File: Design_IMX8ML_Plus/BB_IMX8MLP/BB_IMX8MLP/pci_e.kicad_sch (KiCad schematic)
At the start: 0 parts

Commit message: Add SPB228 WIFI/BLE module
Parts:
- added J8: Bus_PCI_Express_Mini, Connector_PCBEdge:BUS_PCI_Express_Mini, symbol Connector:Bus_PCI_Express_Mini
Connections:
- new net: J8.15 (GND), J8.18 (GND), J8.21 (GND), J8.26 (GND), J8.27 (GND), J8.29 (GND), J8.34 (GND), J8.35 (GND), J8.37 (GND), J8.4 (GND), J8.40 (GND), J8.43 (GND), J8.50 (GND), J8.9 (GND)
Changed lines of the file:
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@@
-(kicad_sch (version 20230121) (generator eeschema)
-  (paper "A4")
+(kicad_sch
+	(version 20231120)
+	(generator "eeschema")
+	(generator_version "8.0")
+	(paper "A4")
+	(symbol
+		(lib_id "Connector:Bus_PCI_Express_Mini")
+		(at 167.64 107.95 0)
+		(unit 1)
+		(exclude_from_sim no)
+		(in_bom yes)
+		(on_board yes)
+		(dnp no)
+		(fields_autoplaced yes)
+		(property "Reference" "J8"
+			(at 172.3741 138.43 0)
+			(effects
+				(font
+					(size 1.27 1.27)
+				)
+				(justify left)
+			)
+		)
+		(property "Value" "Bus_PCI_Express_Mini"
+			(at 172.3741 140.97 0)
+			(effects
+				(font
+					(size 1.27 1.27)
+				)
+				(justify left)
+			)
+		)
+		(property "Footprint" "Connector_PCBEdge:BUS_PCI_Express_Mini"
+			(at 167.64 107.95 0)
+			(effects
+				(font
+					(size 1.27 1.27)
+				)
+				(hide yes)
+			)
+		)
+		(property "Datasheet" "0679105700"
+			(at 163.83 137.16 0)
+			(effects
+				(font
+					(size 1.27 1.27)
+				)
+				(hide yes)
+			)
+		)
+		(property "Description" "Mini-PCI Express bus connector"
+			(at 167.64 107.95 0)
+			(effects
+				(font
+					(size 1.27 1.27)
+				)
+				(hide yes)
+			)
+		)
+		(pin "23"
+		)
+		(pin "34"
+		)
+		(pin "30"
+		)
+		(pin "MP"
+		)
+		(pin "43"
+		)
+		(pin "20"
+		)
+		(pin "24"
+		)
+		(pin "9"
+		)
+		(pin "7"
+		)
+		(pin "45"
+		)
+		(pin "17"
+		)
+		(pin "44"
+		)
+		(pin "2"
+		)
+		(pin "5"
+		)
+		(pin "36"
+		)
+		(pin "3"
+		)
+		(pin "6"
+		)
+		(pin "25"
+		)
+		(pin "49"
+		)
+		(pin "38"
+		)
+		(pin "22"
+		)
+		(pin "40"
+		)
+		(pin "41"
+		)
+		(pin "39"
+		)
+		(pin "51"
+		)
+		(pin "19"
+		)
+		(pin "35"
+		)
+		(pin "47"
+		)
+		(pin "50"
+		)
+		(pin "29"
+		)
+		(pin "46"
+		)
+		(pin "28"
+		)
+		(pin "37"
+		)
+		(pin "21"
+		)
+		(pin "8"
+		)
+		(pin "42"
+		)
+		(pin "18"
+		)
+		(pin "52"
+		)
+		(pin "26"
+		)
+		(pin "31"
+		)
+		(pin "32"
+		)
+		(pin "33"
+		)
+		(pin "27"
+		)
+		(pin "48"
+		)
+		(pin "4"
+		)
+		(pin "15"
+		)
+		(pin "11"
+		)
+		(pin "10"
+		)
+		(pin "1"
+		)
+		(pin "14"
+		)
+		(pin "13"
+		)
+		(pin "12"
+		)
+		(pin "16"
+		)
+		(instances
+			(project ""
+				(path "/cd2fb234-91e5-476f-84ed-38419b628dc6/d6dc9945-1df7-4624-8f27-7360b0b9c0df"
+					(reference "J8")
+					(unit 1)
+				)
+			)
+		)
+	)
 )

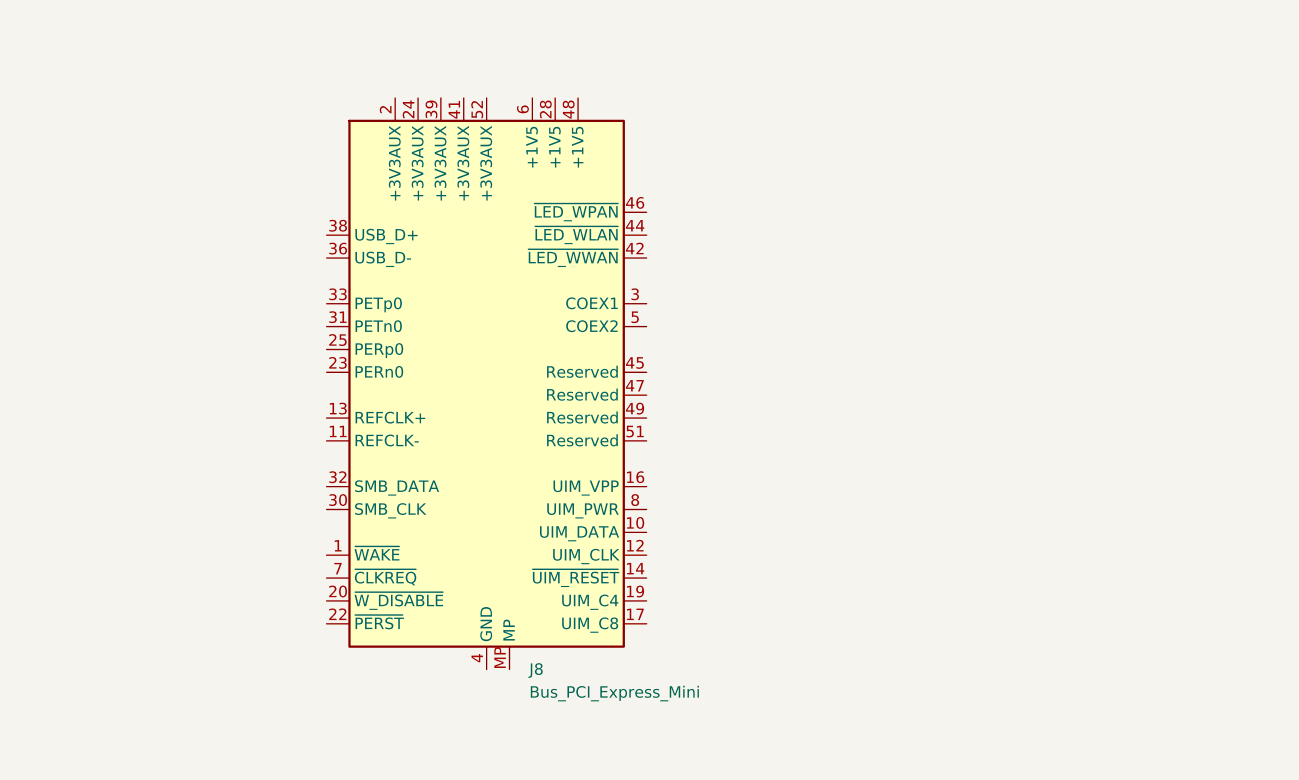
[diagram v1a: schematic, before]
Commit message: Improve power source module in the base board
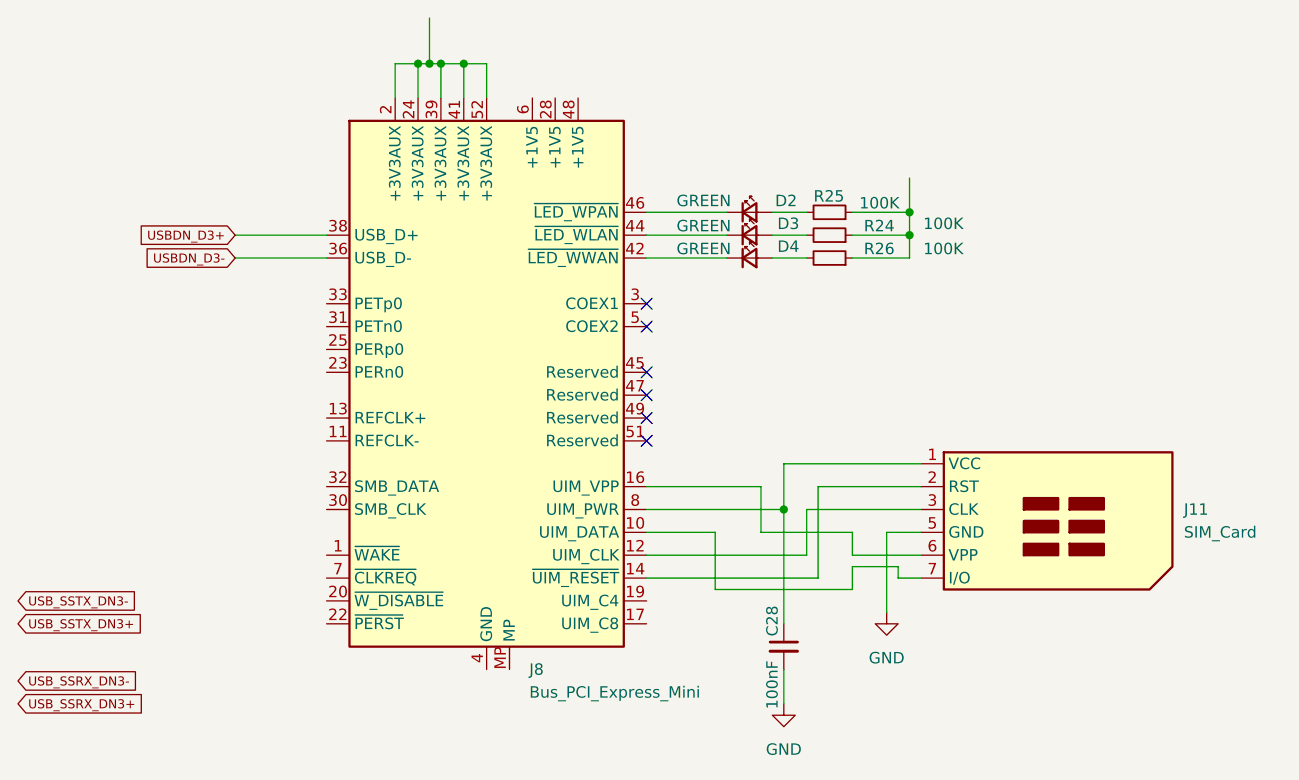
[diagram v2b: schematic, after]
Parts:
- added C28: 100nF, Capacitor_SMD:C_0402_1005Metric, symbol Device:C_Small
- added D2, D3, D4: GREEN, LED_SMD:LED_0402_1005Metric, symbol Device:LED_Small
- added J11: SIM_Card, Connector_Card:nanoSIM_Hinged_CUI_NSIM-2-C, symbol Connector:SIM_Card
- added R24, R25, R26: 100K, Resistor_SMD:R_0402_1005Metric, symbol Device:R_Small
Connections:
- net at J8.10 (UIM_DATA): now also J11.7 (I/O)
- net at J8.12 (UIM_CLK): now also J11.3 (CLK)
- net at J8.14 (~{UIM_RESET}): now also J11.2 (RST)
- net at J8.16 (UIM_VPP): now also J11.6 (VPP)
- net at J8.2 (+3V3AUX): now also J8.24 (+3V3AUX), J8.39 (+3V3AUX), J8.41 (+3V3AUX), J8.52 (+3V3AUX)
- net USBDN_D3-: now reaches J8.36 (USB_D-)
- net USBDN_D3+: now reaches J8.38 (USB_D+)
- net at J8.42 (~{LED_WWAN}): now also D4.1 (K)
- net at J8.44 (~{LED_WLAN}): now also D3.1 (K)
- net at J8.46 (~{LED_WPAN}): now also D2.1 (K)
- net at J8.8 (UIM_PWR): now also C28.1, J11.1 (VCC)
- new net: D3.2 (A), R25.2
- new net: R24.1, R25.1, R26.1
- new net: D2.2 (A), R24.2
- new net: D4.2 (A), R26.2
- new net GND: C28.2, J11.5 (GND)
- no-connect marks 0 -> 6

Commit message: improving the usb conector
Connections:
- net PCIE_REF_PAD_CLK_N: now reaches J8.11 (REFCLK-)
- net PCIE_REF_PAD_CLK_P: now reaches J8.13 (REFCLK+)
- net PCIE_RXN_N: now reaches J8.23 (PERn0)
- net PCIE_RXN_P: now reaches J8.25 (PERp0)
- net at J8.28 (+1V5): now also J8.48 (+1V5), J8.6 (+1V5)
- net PCIE_TXN_N: now reaches J8.31 (PETn0)
- net PCIE_TXN_P: now reaches J8.33 (PETp0)
- no-connect marks 6 -> 7

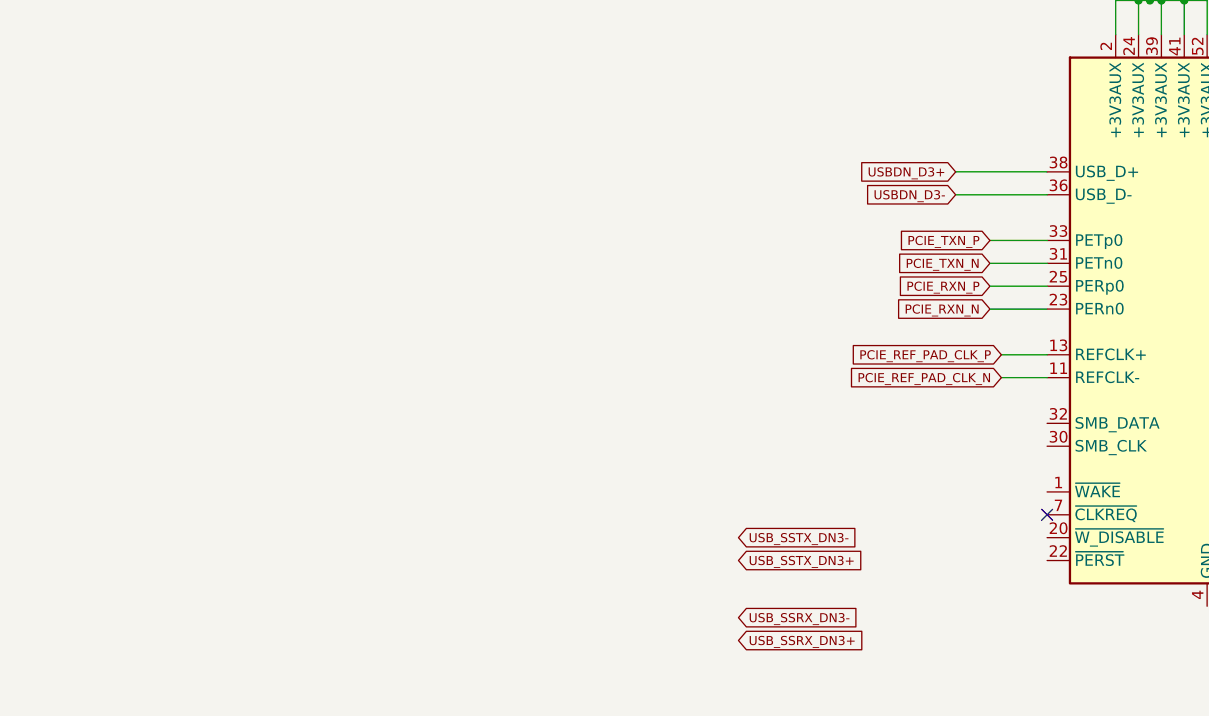
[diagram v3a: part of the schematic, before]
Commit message: improving Ethernet, USB and Camera inteface
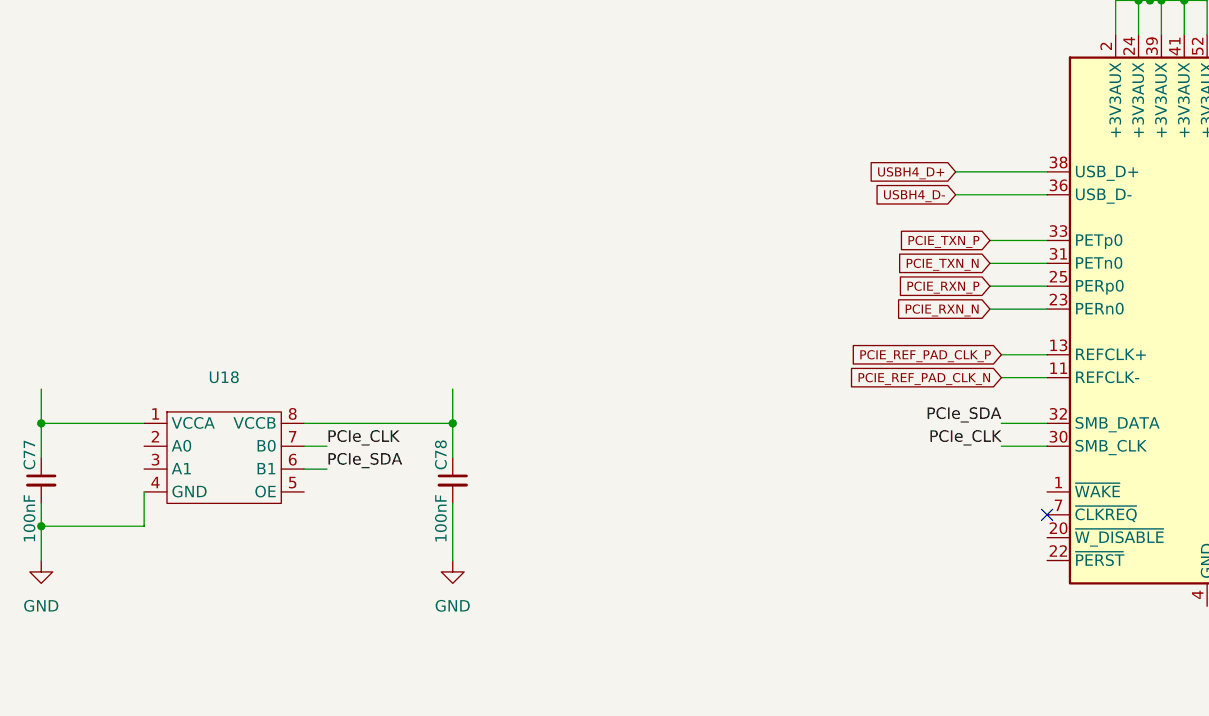
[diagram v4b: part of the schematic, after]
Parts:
- added C77, C78: 100nF, Capacitor_SMD:C_0402_1005Metric, symbol Device:C_Small
- added U18: ~, _W_SBC:MICROPAK8_1P6X1P6_ONS, symbol _W_MX8M:FXMA2102L8X
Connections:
- net GND: now also C77.2, C78.2, U18.4 (GND)
- net PCIe_CLK: now reaches J8.30 (SMB_CLK)
- net PCIe_CLK: now also U18.7 (B0)
- net PCIe_SDA: now reaches J8.32 (SMB_DATA)
- net PCIe_SDA: now also U18.6 (B1)
- net USBDN_D3+ renamed USBH4_D+
- net USBDN_D3- renamed USBH4_D-
- new net: C77.1, U18.1 (VCCA)
- new net: C78.1, U18.8 (VCCB)

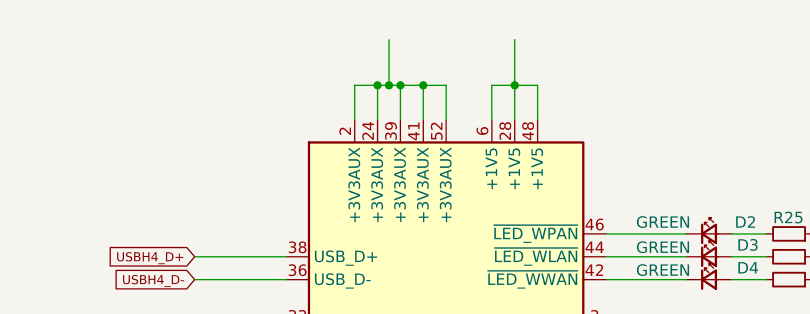
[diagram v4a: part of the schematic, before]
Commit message: Add LVDs and CSI Interface
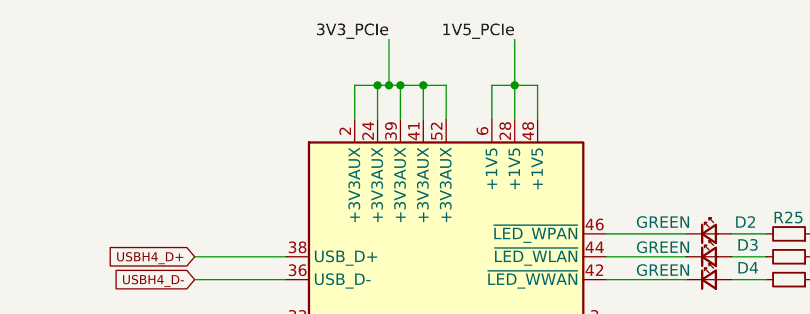
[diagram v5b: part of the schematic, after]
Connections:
- net 3V3_PCIe: now reaches J8.2 (+3V3AUX), J8.24 (+3V3AUX), J8.39 (+3V3AUX), J8.41 (+3V3AUX), J8.52 (+3V3AUX)
- net 1V5_PCIe: now reaches J8.28 (+1V5), J8.48 (+1V5), J8.6 (+1V5)
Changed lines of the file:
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@@
+		)
+	)
+	(label "3V3_PCIe"
+		(at 161.29 66.04 180)
+		(effects
+			(font
+				(size 1.27 1.27)
+			)
+			(justify right bottom)
 		)
 	)
@@
 		)
 	)
+	(label "1V5_PCIe"
+		(at 175.26 66.04 180)
+		(effects
+			(font
+				(size 1.27 1.27)
+			)
+			(justify right bottom)
+		)
+	)

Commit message: Review
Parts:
- added C154: 100pF, Capacitor_SMD:C_0402_1005Metric, symbol Device:C_Small
- added C155: 1nF, Capacitor_SMD:C_0402_1005Metric, symbol Device:C_Small
- added C156: 100nF, Capacitor_SMD:C_0402_1005Metric, symbol Device:C_Small
- added J22: SD_Card_Receptacle, symbol Connector:SD_Card_Receptacle
- added R62, R63: 10K, Resistor_SMD:R_0402_1005Metric, symbol Device:R_Small
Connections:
- net GND: now also C154.2, C155.2, C156.2, J22.3 (VSS), J22.6 (VSS)
- net PCIe_CLK: now also R62.2
- net PCIe_SDA: now also R63.2
- net 1v8: now reaches C77.1, U18.1 (VCCA)
- net I2C1_SCL: now reaches U18.2 (A0)
- net I2C1_SDA: now reaches U18.3 (A1)
- net 3v3: now reaches C78.1, U18.8 (VCCB)
- net 3v3: now also C154.1, C155.1, C156.1, J22.4 (VDD), R62.1, R63.1
- new net SDC2_CD_B: J22.10 (CARD_DETECT)
- new net SDC2_CLK: J22.5 (CLK)
- new net SDC2_CMD: J22.2 (CMD)
- new net SDC2_DATA0: J22.7 (DAT0)
- new net SDC2_DATA1: J22.8 (DAT1)
- new net SDC2_DATA2: J22.9 (DAT2)
- new net SDC2_DATA3: J22.1 (CD/DAT3)
- no-connect marks 7 -> 8
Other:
- moved on the sheet: C28, C77, C78, D2, D3, D4, J11, J8, R24, R25, R26

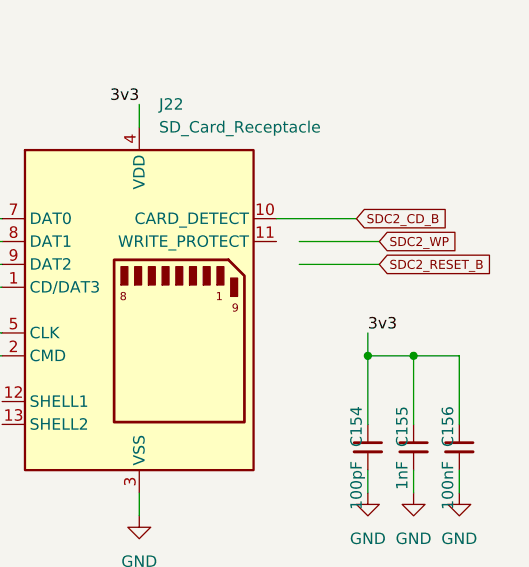
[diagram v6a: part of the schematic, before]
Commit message: reorganization of the componentes
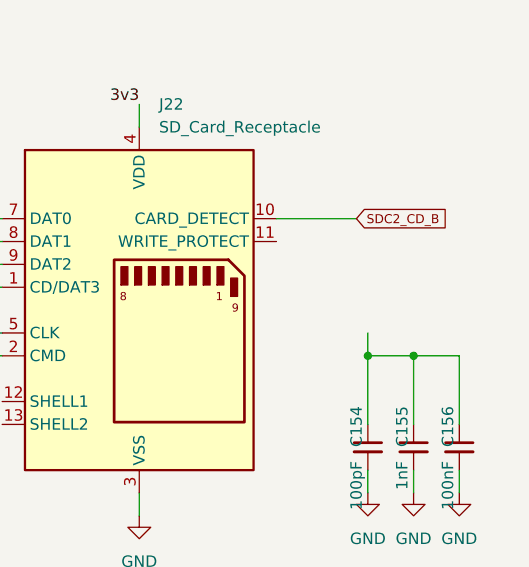
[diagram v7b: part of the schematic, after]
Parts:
- J22: footprint (none) -> Connector_Card:SD_Hirose_DM1AA_SF_PEJ82
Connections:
- net 3v3: no longer C154.1, C155.1, C156.1
- new net: C154.1, C155.1, C156.1
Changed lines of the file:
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@@
 	(wire
 		(pts
-			(xy 246.38 127) (xy 255.27 127)
-		)
-		(stroke
-			(width 0)
-			(type default)
-		)
-	)
-	(wire
-		(pts
 			(xy 144.78 46.99) (xy 151.13 46.99)
 		)
@@
 	(wire
 		(pts
-			(xy 246.38 129.54) (xy 255.27 129.54)
-		)
-		(stroke
-			(width 0)
-			(type default)
-		)
-	)
-	(wire
-		(pts
 			(xy 72.39 118.11) (xy 72.39 125.73)
 		)
@@
 		)
 	)
-	(label "3v3"
-		(at 254 137.16 0)
-		(effects
-			(font
-				(size 1.27 1.27)
-			)
-			(justify left bottom)
-		)
-	)
 	(label "PCIe_CLK"
 		(at 105.41 142.24 0)
@@
 		)
 	)
-	(global_label "SDC2_RESET_B"
-		(shape input)
-		(at 255.27 129.54 0)
-		(fields_autoplaced yes)
-		(effects
-			(font
-				(size 1 1)
-			)
-			(justify left)
-		)
-		(property "Intersheetrefs" "${INTERSHEET_REFS}"
-			(at 268.5104 129.54 0)
-			(effects
-				(font
-					(size 1.27 1.27)
-				)
-				(justify left)
-				(hide yes)
-			)
-		)
-	)
 	(global_label "SDC2_CD_B"
 		(shape input)
@@
 		)
 	)
-	(global_label "SDC2_WP"
-		(shape input)
-		(at 255.27 127 0)
-		(fields_autoplaced yes)
-		(effects
-			(font
-				(size 1 1)
-			)
-			(justify left)
-		)
-		(property "Intersheetrefs" "${INTERSHEET_REFS}"
-			(at 264.3675 127 0)
-			(effects
-				(font
-					(size 1.27 1.27)
-				)
-				(justify left)
-				(hide yes)
-			)
-		)
-	)
 	(global_label "SDC2_CLK"
 		(shape input)
@@
 			)
 		)
-		(property "Footprint" ""
+		(property "Footprint" "Connector_Card:SD_Hirose_DM1AA_SF_PEJ82"
 			(at 237.49 137.922 0)
 			(effects

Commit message: CPU Board actualizate
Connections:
- net 3v3: no longer J22.4 (VDD)
- net +3.3V: now reaches C154.1, C155.1, C156.1
- net +3.3V: now also J22.4 (VDD)
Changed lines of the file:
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@@
-		)
-	)
-	(label "3v3"
-		(at 228.6 111.76 180)
-		(effects
-			(font
-				(size 1.27 1.27)
-			)
-			(justify right bottom)
 		)
 	)
@@
 	)
 	(symbol
+		(lib_id "power:+3.3V")
+		(at 228.6 111.76 0)
+		(unit 1)
+		(exclude_from_sim no)
+		(in_bom yes)
+		(on_board yes)
+		(dnp no)
+		(fields_autoplaced yes)
+		(property "Reference" "#PWR8"
+			(at 228.6 115.57 0)
+			(effects
+				(font
+					(size 1.27 1.27)
+				)
+				(hide yes)
+			)
+		)
+		(property "Value" "+3.3V"
+			(at 228.6 106.68 0)
+			(effects
+				(font
+					(size 1.27 1.27)
+				)
+			)
+		)
+		(property "Footprint" ""
+			(at 228.6 111.76 0)
+			(effects
+				(font
+					(size 1.27 1.27)
+				)
+				(hide yes)
+			)
+		)
+		(property "Datasheet" ""
+			(at 228.6 111.76 0)
+			(effects
+				(font
+					(size 1.27 1.27)
+				)
+				(hide yes)
+			)
+		)
+		(property "Description" "Power symbol creates a global label with name \"+3.3V\""
+			(at 228.6 111.76 0)
+			(effects
+				(font
+					(size 1.27 1.27)
+				)
+				(hide yes)
+			)
+		)
+		(pin "1"
+		)
+		(instances
+			(project "BB_IMX8MLP"
+				(path "/cd2fb234-91e5-476f-84ed-38419b628dc6/d6dc9945-1df7-4624-8f27-7360b0b9c0df"
+					(reference "#PWR8")
+					(unit 1)
+				)
+			)
+		)
+	)
+	(symbol
 		(lib_id "Device:R_Small")
 		(at 142.24 44.45 270)
@@
 	)
 	(symbol
+		(lib_id "power:+3.3V")
+		(at 254 137.16 0)
+		(unit 1)
+		(exclude_from_sim no)
+		(in_bom yes)
+		(on_board yes)
+		(dnp no)
+		(fields_autoplaced yes)
+		(property "Reference" "#PWR112"
+			(at 254 140.97 0)
+			(effects
+				(font
+					(size 1.27 1.27)
+				)
+				(hide yes)
+			)
+		)
+		(property "Value" "+3.3V"
+			(at 254 132.08 0)
+			(effects
+				(font
+					(size 1.27 1.27)
+				)
+			)
+		)
+		(property "Footprint" ""
+			(at 254 137.16 0)
+			(effects
+				(font
+					(size 1.27 1.27)
+				)
+				(hide yes)
+			)
+		)
+		(property "Datasheet" ""
+			(at 254 137.16 0)
+			(effects
+				(font
+					(size 1.27 1.27)
+				)
+				(hide yes)
+			)
+		)
+		(property "Description" "Power symbol creates a global label with name \"+3.3V\""
+			(at 254 137.16 0)
+			(effects
+				(font
+					(size 1.27 1.27)
+				)
+				(hide yes)
+			)
+		)
+		(pin "1"
+		)
+		(instances
+			(project "BB_IMX8MLP"
+				(path "/cd2fb234-91e5-476f-84ed-38419b628dc6/d6dc9945-1df7-4624-8f27-7360b0b9c0df"
+					(reference "#PWR112")
+					(unit 1)
+				)
+			)
+		)
+	)
+	(symbol
 		(lib_id "power:GND")
 		(at 228.6 157.48 0)
@@
 			)
 		)
-		(property "Datasheet" "0679105700"
+		(property "Datasheet" "~"
 			(at 100.33 93.98 0)
 			(effects
